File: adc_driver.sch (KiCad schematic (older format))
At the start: 32 parts, among them U17 DG412xUE, U18 AD8421ARZ, U22 TMUX6136PWR, U24 LMP8350MA_NOPB

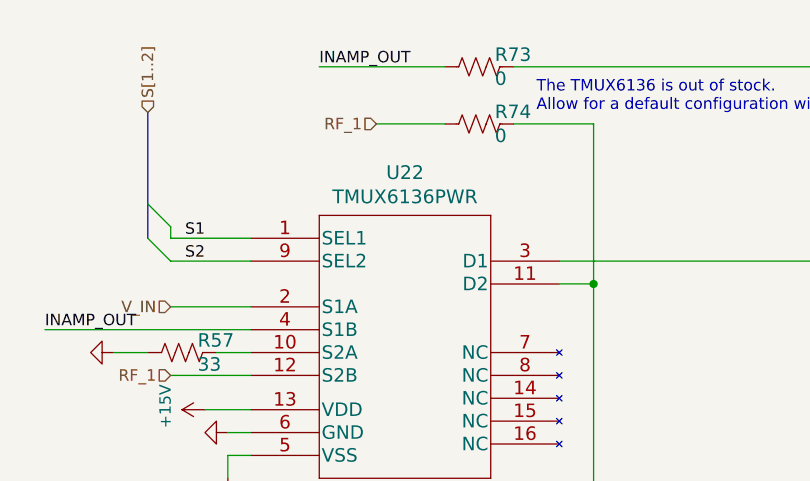
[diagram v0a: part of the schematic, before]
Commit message: gerbers, BOM and fabrication files sent to PCBway
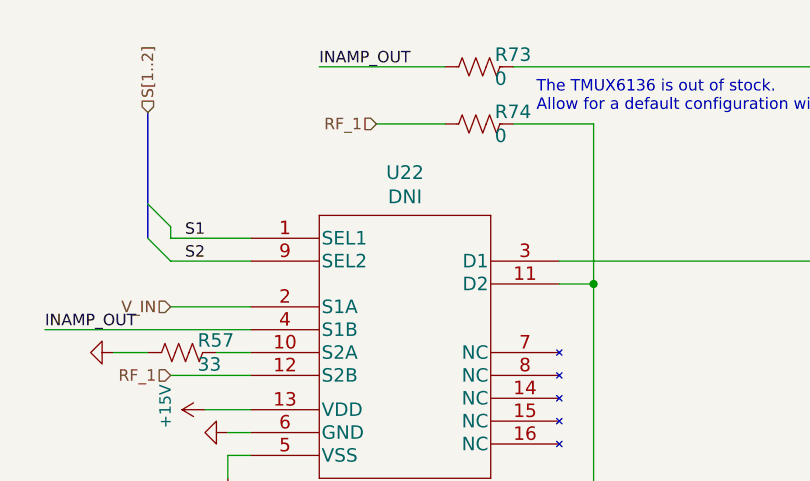
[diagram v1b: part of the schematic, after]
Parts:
- U22: value TMUX6136PWR -> DNI
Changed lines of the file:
@@
 P 3150 1450
 F 0 "U22" H 3825 1737 60  0000 C CNN
-F 1 "TMUX6136PWR" H 3825 1631 60  0000 C CNN
+F 1 "DNI" H 3825 1631 60  0000 C CNN
 F 2 "Package_SO:TSSOP-16_4.4x5mm_P0.65mm" H 3800 1550 60  0001 C CNN
 F 3 "" H 3150 1450 60  0000 C CNN

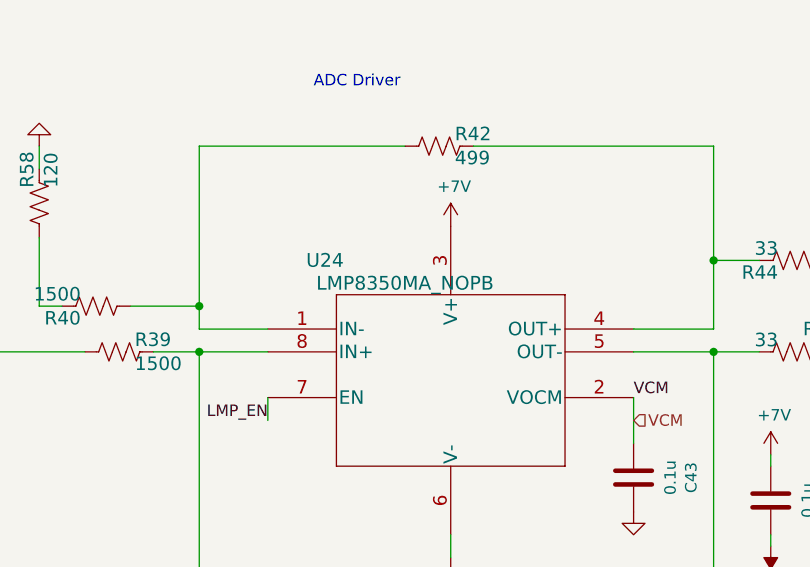
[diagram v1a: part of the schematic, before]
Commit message: add PDF print of schematic
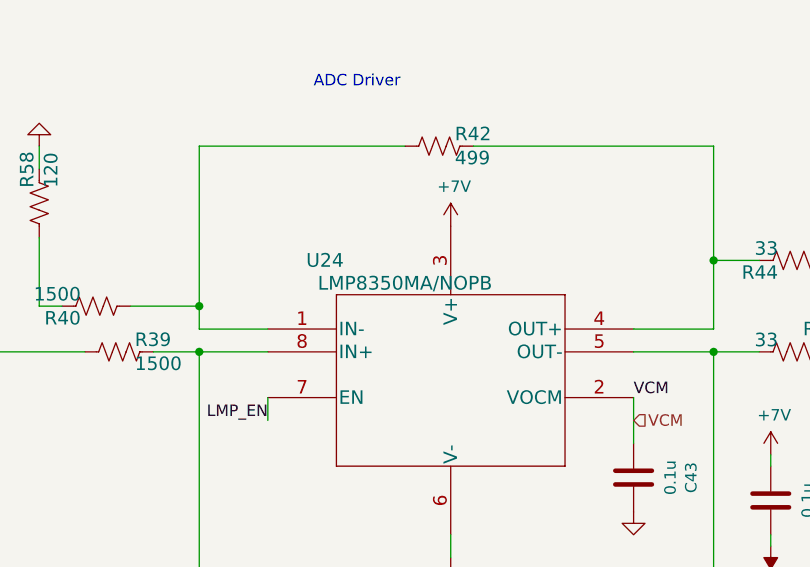
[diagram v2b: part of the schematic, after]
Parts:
- U24: value LMP8350MA_NOPB -> LMP8350MA/NOPB; Alternate Manf# LMP8350MA/NOPB -> LMP8350MAX/NOPB; Manf# LMP8350MAX/NOPB -> LMP8350MA/NOPB
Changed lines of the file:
@@
 P 7700 3650
 F 0 "U24" H 7950 3750 60  0000 C CNN
-F 1 "LMP8350MA_NOPB" H 8300 3650 60  0000 C CNN
+F 1 "LMP8350MA/NOPB" H 8300 3650 60  0000 C CNN
 F 2 "Package_SO:SOIC-8_3.9x4.9mm_P1.27mm" H 8200 3750 60  0001 C CNN
 F 3 "" H 7700 3650 60  0000 C CNN
-F 4 "LMP8350MAX/NOPB" H 7700 3650 50  0001 C CNN "Manf#"
-F 5 "LMP8350MA/NOPB" H 7700 3650 50  0001 C CNN "Alternate Manf#"
+F 4 "LMP8350MA/NOPB" H 7700 3650 50  0001 C CNN "Manf#"
+F 5 "LMP8350MAX/NOPB" H 7700 3650 50  0001 C CNN "Alternate Manf#"
 F 6 "AD8138AARZ-R7" H 7700 3650 50  0001 C CNN "Alternate2 Manf#"
 	1    7700 3650
